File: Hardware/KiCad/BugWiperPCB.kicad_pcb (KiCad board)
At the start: 4 copper layers, 110 x 40 mm, 100 parts, among them J1 UJ20-C-H-G-SMT-1-P16-TR, J2 1770924, J3 Phoenix_1776508, J4 RJ45, J5 Conn_TagConnect_TC2030-NL_ESP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, J6 1824420000, Q1 NMOS_SO-8, U1 ESP32-S3-WROOM-1, U2 BTN9960LV, U3 BTN9960LV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

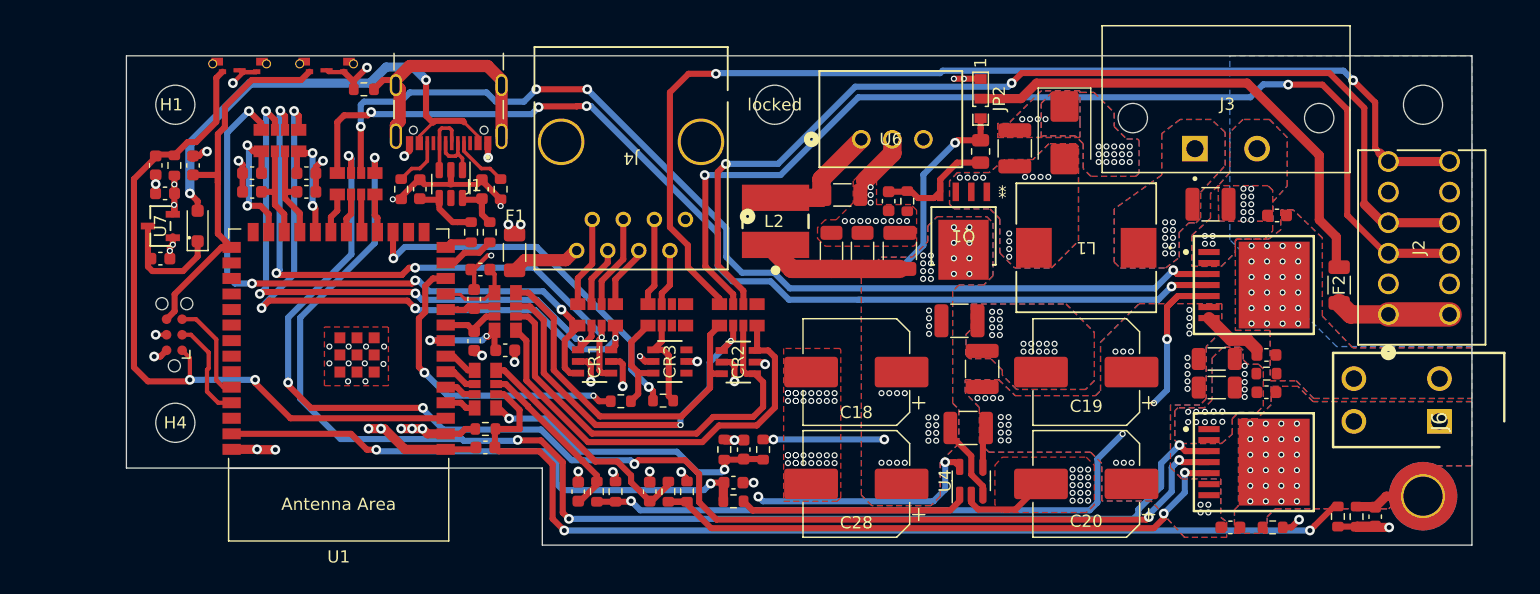
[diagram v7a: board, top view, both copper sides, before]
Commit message: Update PCB
add Connector for Sw_2, add voltage devider for the encoder
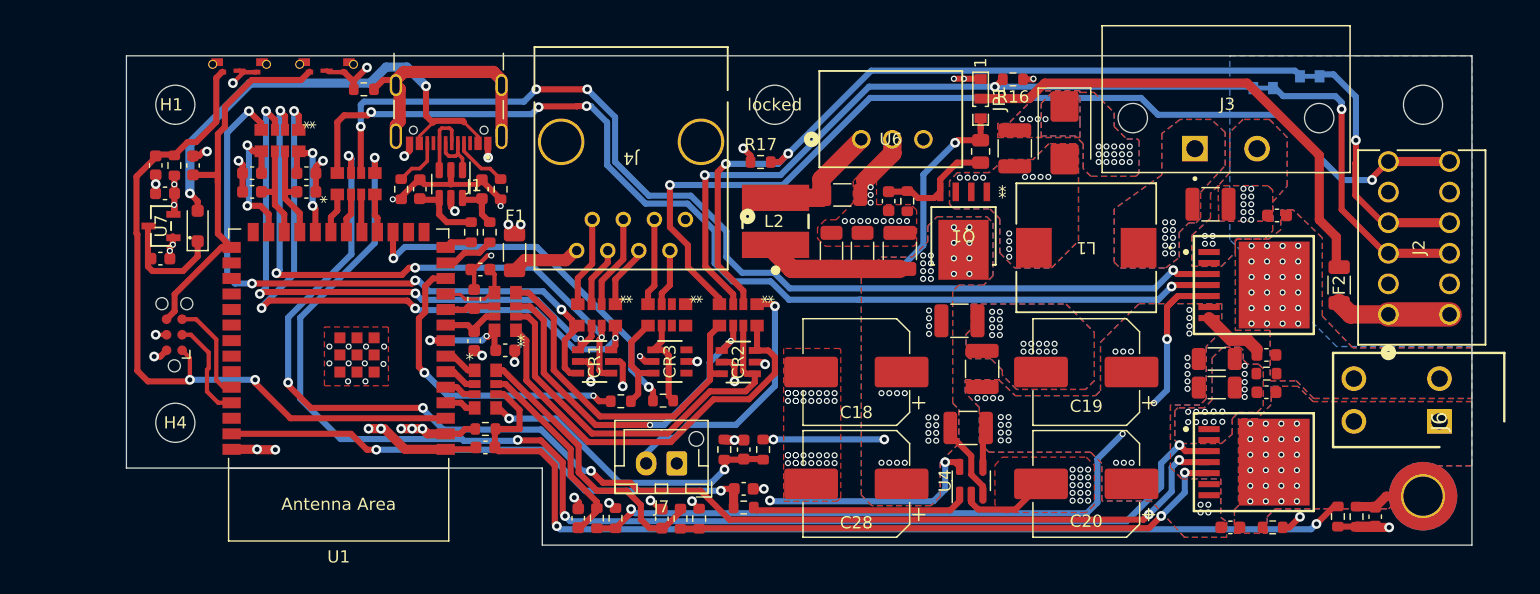
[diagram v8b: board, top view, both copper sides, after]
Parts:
- added J7: Conn_01x02_Pin, Connector_JST:JST_XH_B2B-XH-AM_1x02_P2.50mm_Vertical, F.Cu at (155.0, 93.3)
- added JP2: Bridged 12, BugWiper_lib:SolderJumper_2P_R_SMD_0603_Bridged, B.Cu at (205.9, 61.7)
- added JP3: Bridged 12, BugWiper_lib:SolderJumper_2P_R_SMD_0603_Bridged, B.Cu at (202.1, 62.6)
- added R16: ~, Resistor_SMD:R_0603_1608Metric, F.Cu at (182.5, 61.9)
- added R17: ~, Resistor_SMD:R_0603_1608Metric, F.Cu at (161.8, 68.7)
- moved C11 2.42 mm to (153.8, 97.8)
- moved R10 2.42 mm to (155.3, 97.8)
- moved R9 2.42 mm to (156.8, 97.8)
- moved C12 2.17 mm to (146.9, 97.8)
- moved R11 2.17 mm to (148.5, 97.8)
- moved R12 2.17 mm to (150.0, 97.8)
- moved C22 0.98 mm to (160.5, 95.4)
- moved R13 0.98 mm to (160.5, 96.9)
- moved U7 0.05 mm to (112.8, 73.9)
- renumbered JP2 to JP1
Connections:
- RN7 pad 1: /ESP32-S3/sw_2 -> sw_2
- RN7 pad 2: EN_C1 -> Enc_1
- RN7 pad 3: EN_C2 -> Enc_2
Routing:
- net Enc_1: track 0.00 -> 64.4 mm, vias 0 -> 2
- net EN_C1: track 84.5 -> 20.3 mm, vias 2 -> 1
- net EN_C2: track 86.3 -> 25.0 mm, vias 2 -> 1
- net Enc_2: track 0.00 -> 60.1 mm, vias 0 -> 2
- net sw_2: track 0.00 -> 21.7 mm, vias 0 -> 1
- net sw_1: track 88.7 -> 81.6 mm
- net /ESP32-S3/M_IS1: track 19.7 -> 23.2 mm
- net GND: track 85.3 -> 88.0 mm, vias 168 -> 170
- net Net-(U2-IS): track 49.9 -> 47.5 mm
- net /ESP32-S3/M_IS2: track 14.3 -> 16.4 mm
- net Net-(CR2-IO_3): track 35.4 -> 33.2 mm
- net /ESP32-S3/M_IHN2: track 85.1 -> 87.1 mm
- net /ESP32-S3/M_INH1: track 107.5 -> 105.8 mm
- net Net-(CR2-IO_4): track 36.1 -> 34.5 mm
- net /ESP32-S3/M_IN2: track 84.9 -> 86.3 mm
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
